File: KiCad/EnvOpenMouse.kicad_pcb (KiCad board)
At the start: 2 copper layers, 28.6 x 94.8 mm, 58 parts, among them J8 TSA343G00-250J2, J9 C145960, Q1 SI2301B, SW1 SW_Push_SPDT, SW2 SW_Push_SPDT, SW3 SW_Push_SPDT, U1 TLV70218DBVR, U2 PMW3360DM-T2QU, U3 SOT-23-5 5.5V 3.3V 500mA, U4 RP2040, Y1 3225_4P

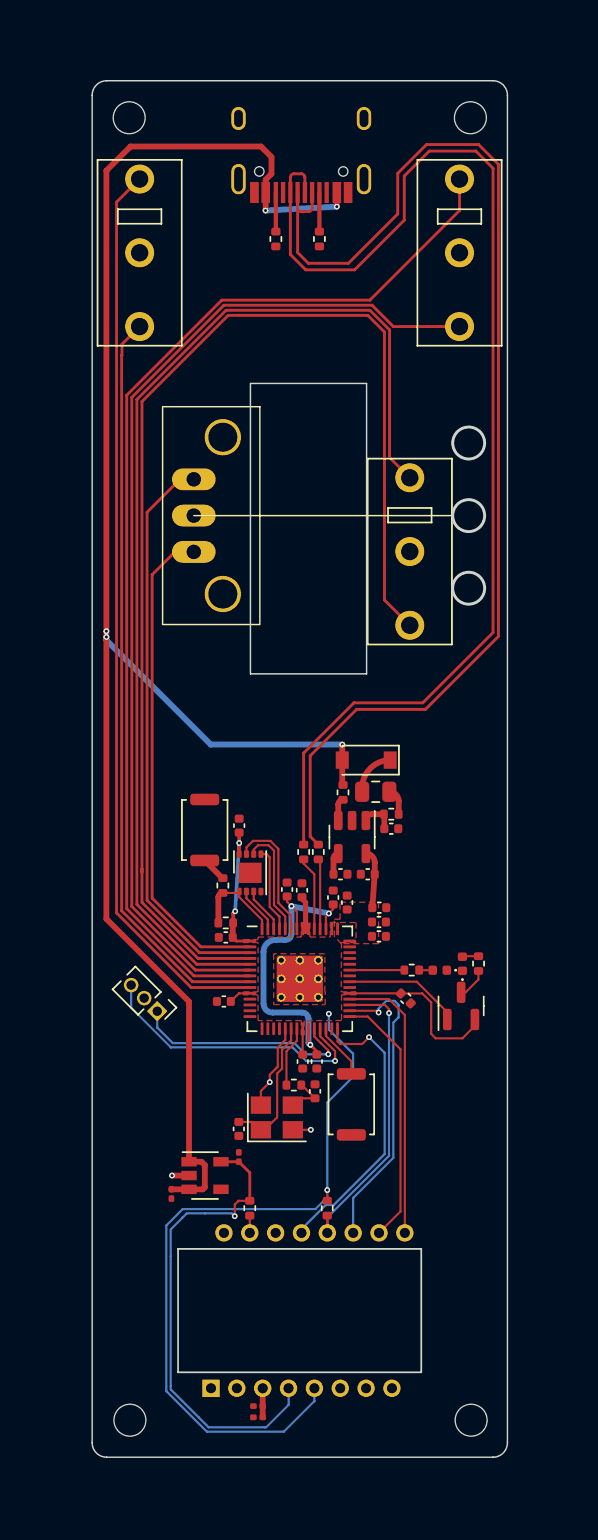
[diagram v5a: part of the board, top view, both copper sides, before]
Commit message: Decided to re-design the whole board again but with a pico so perhaps I can fit a PicoW and maybe make a BLE version
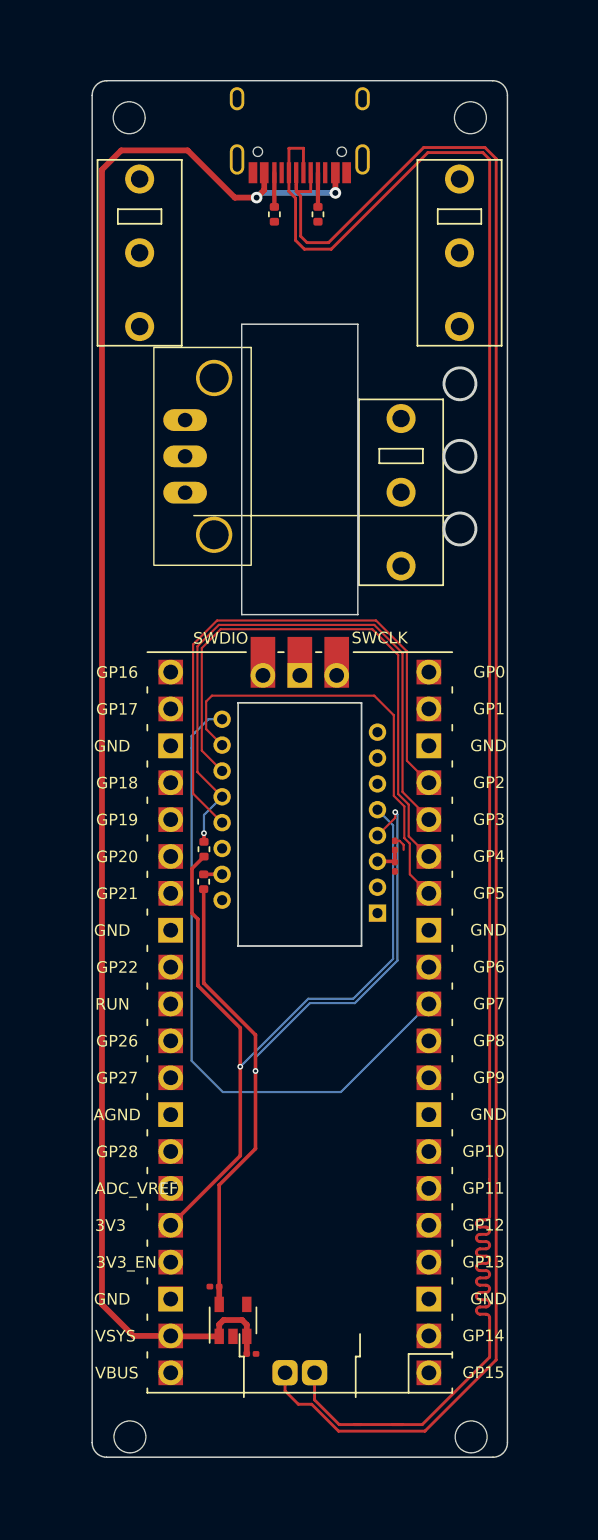
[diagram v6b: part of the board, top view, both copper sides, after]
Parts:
- removed C10, C11, C12, C13, C14, C15, C16, C19, C8, C9: 100nf 0402, Capacitor_SMD:C_0402_1005Metric
- removed C17, C18: 1uf 0402, Capacitor_SMD:C_0402_1005Metric
- removed C20, C5, C6, CBP1: 10uf 0402, Capacitor_SMD:C_0402_1005Metric
- removed C21, C22: 22pf 0402, Capacitor_SMD:C_0402_1005Metric
- removed D1: 1N4002W, Diode_SMD:D_SOD-123
- removed F1: 0805L050WR, Fuse:Fuse_0805_2012Metric
- removed FB1: FerriteBead 0402, Resistor_SMD:R_0402_1005Metric
- removed FLASH1: W25Q16JVUXIQ, Package_SON:SON-8-1EP_3x2mm_P0.5mm_EP1.4x1.6mm
- removed GP23_LED1: GP23 LED_0402, LED_SMD:LED_0402_1005Metric
- removed GPIO24_RESISTOR1, R14, R15: 1K 0402, Resistor_SMD:R_0402_1005Metric
- removed GPIO25_LED1: LED_0402, LED_SMD:LED_0402_1005Metric
- removed GPIO25_RESISTOR1: 470 0402, Resistor_SMD:R_0402_1005Metric
- removed J8, RSW1: TSA343G00-250J2, Button_Switch_SMD:SW_Push_SPST_NO_Alps_SKRK
- removed J9: C145960, Connector_PinHeader_1.27mm:PinHeader_1x03_P1.27mm_Vertical
- removed Q1: SI2301B, Package_TO_SOT_SMD:SOT-23
- removed R11, R12: 27r 0402 resistor, Resistor_SMD:R_0402_1005Metric
- removed R13: 10K 0402, Resistor_SMD:R_0402_1005Metric
- removed R3, R7: 5.1K 0402, Resistor_SMD:R_0402_1005Metric
- removed R8: 100K 0402, Resistor_SMD:R_0402_1005Metric
- removed U3: SOT-23-5 5.5V 3.3V 500mA, Package_TO_SOT_SMD:SOT-23-5
- removed U4: RP2040, RP2040_minimal:RP2040-QFN-56
- removed USB1: TYPE-C-31-M-12, HRO-TYPE-C31-M-12:HRO-TYPE-C-31-M-12
- removed Y1: 3225_4P, Crystal:Crystal_SMD_3225-4Pin_3.2x2.5mm
- added R101: 5.1K 0402, Resistor_SMD:R_0402_1005Metric, F.Cu at (44.5, 29.9)
- added R102: 5.1K 0402, Resistor_SMD:R_0402_1005Metric, F.Cu at (41.5, 29.9)
- added U101: Pico, env:RPi_Pico_SMD_TH_MODIFIED, F.Cu at (43.3, 85.6)
- added USB101: HRO-TYPE-C-31-M-12, Type-C:HRO-TYPE-C-31-M-12, F.Cu at (43.3, 19.4)
- moved C4 40.5 mm to (49.8, 73.4), turned to 90 degrees
- moved C3 38.3 mm to (49.9, 74.9), turned to -90 degrees
- moved U2 32.4 mm to (47.5, 79.6), turned to 180 degrees
- moved R2 26.1 mm to (36.7, 73.7), turned to 90 degrees
- moved R1 22.7 mm to (36.7, 75.9), turned to 90 degrees
- moved C1 12.3 mm to (40.0, 108.4), turned to 180 degrees
- moved U1 10.2 mm to (38.7, 106.1), turned to 90 degrees
- moved C2 9.07 mm to (37.4, 103.8), turned to 0 degrees
- moved SW1 4.12 mm to (50.3, 49.1)
- moved VR1 4.12 mm to (35.4, 46.6)
- moved H3 1.15 mm to (55.1, 114.2)
- moved H4 1.15 mm to (31.6, 114.2)
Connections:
- net MISO/GPIO4 renamed MISO
- U2 pad 10: SCLK/GPIO2 -> SCLK
- U2 pad 11: MOSI/GPIO3 -> MOSI
- U2 pad 13: NCS/GPIO9 -> NCS
- U2 pad 9: MOTION/GPIO1 -> MOTION
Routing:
- net MB-1-A: track 84.3 -> 0.00 mm
- net MB-2-B: track 76.1 -> 0.00 mm
- net MB-1-B: track 75.5 -> 0.00 mm
- net MB-2-A: track 70.8 -> 0.00 mm
- net MB-3-B: track 62.5 -> 0.00 mm
- net USB_D+: track 82.4 -> 137.6 mm
- net MB-3-A: track 51.6 -> 0.00 mm
- net MOTION: track 0.00 -> 44.7 mm
- net USB_D-: track 82.5 -> 125.6 mm
- net ROT-A: track 39.5 -> 0.00 mm
- net NCS: track 0.00 -> 39.1 mm
- net MOSI: track 0.00 -> 38.6 mm
- net ROT-B: track 33.9 -> 0.00 mm
- net SCLK: track 0.00 -> 30.4 mm
- net +3V3: track 82.4 -> 53.4 mm, vias 4 -> 1
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- removed copper zone on F.Cu, net +3V3
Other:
- outline, holes or cut-outs redrawn

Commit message: routed and adjusted various traces and component positions
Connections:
- U101 pad 21: unconnected-(U101-GPIO16-Pad21) -> ROT-B
- U101 pad 22: unconnected-(U101-GPIO17-Pad22) -> ROT-A
- U101 pad 24: unconnected-(U101-GPIO18-Pad24) -> MB-1-A
- U101 pad 25: unconnected-(U101-GPIO19-Pad25) -> MB-1-B
- U101 pad 26: unconnected-(U101-GPIO20-Pad26) -> MB-2-A
- U101 pad 27: unconnected-(U101-GPIO21-Pad27) -> MB-2-B
- U101 pad 29: unconnected-(U101-GPIO22-Pad29) -> MB-3-A
- U101 pad 31: unconnected-(U101-GPIO26_ADC0-Pad31) -> MB-3-B
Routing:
- net MB-2-B: track 0.00 -> 66.0 mm
- net MB-1-A: track 0.00 -> 65.3 mm
- net MB-3-B: track 0.00 -> 62.8 mm
- net MB-2-A: track 0.00 -> 60.0 mm
- net MB-1-B: track 0.00 -> 59.0 mm
- net MB-3-A: track 0.00 -> 47.0 mm
- net ROT-A: track 0.00 -> 22.6 mm
- net ROT-B: track 0.00 -> 13.8 mm
- net MOSI: track 38.6 -> 30.2 mm
- net USB_D+: track 137.6 -> 140.6 mm
- net USB_D-: track 125.6 -> 128.4 mm
- net NCS: track 39.1 -> 38.5 mm
- net MISO: track 42.4 -> 41.9 mm
- net GND: vias 0 -> 2
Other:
- board text added: "Envious.Design"
- board text added: "env"

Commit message: overhauled design and generated gerbers
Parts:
- removed R101, R102: 5.1K 0402, Resistor_SMD:R_0402_1005Metric
- removed U101: Pico, env:RPi_Pico_SMD_TH_MODIFIED
- removed USB101: HRO-TYPE-C-31-M-12, Type-C:HRO-TYPE-C-31-M-12
- added BT1: Li-Po Battery, Connector_JST:JST_PH_B2B-PH-K_1x02_P2.00mm_Vertical, F.Cu at (48.9, 79.3)
- added C10: 100nf 0402, Capacitor_SMD:C_0402_1005Metric, F.Cu at (59.8, 33.5)
- added C11: 100nf 0402, Capacitor_SMD:C_0402_1005Metric, F.Cu at (61.3, 34.9)
- added C12: 100nf 0402, Capacitor_SMD:C_0402_1005Metric, F.Cu at (63.4, 47.7)
- added C13: 100nf 0402, Capacitor_SMD:C_0402_1005Metric, F.Cu at (67.6, 39.0)
- added C14: 100nf 0402, Capacitor_SMD:C_0402_1005Metric, F.Cu at (70.8, 43.7)
- added C15: 100nf 0402, Capacitor_SMD:C_0402_1005Metric, F.Cu at (62.4, 47.7)
- added C16: 100nf 0402, Capacitor_SMD:C_0402_1005Metric, F.Cu at (55.8, 42.9)
- added C17: 100nf 0402, Capacitor_SMD:C_0402_1005Metric, F.Cu at (57.4, 38.8)
- added C18: 100nf 0402, Capacitor_SMD:C_0402_1005Metric, F.Cu at (62.3, 35.0)
- added C19: 100nf 0402, Capacitor_SMD:C_0402_1005Metric, F.Cu at (67.6, 38.0)
- added C20: 1uf 0402, Capacitor_SMD:C_0402_1005Metric, F.Cu at (65.4, 36.8)
- added C21: 1uf 0402, Capacitor_SMD:C_0402_1005Metric, F.Cu at (64.5, 36.8)
- added C22: 22pf 0402, Capacitor_SMD:C_0402_1005Metric, F.Cu at (63.5, 50.8)
- added C23: 22pf 0402, Capacitor_SMD:C_0402_1005Metric, F.Cu at (60.2, 54.1)
- added C5: 10uf 0402 6.3V, Capacitor_SMD:C_0402_1005Metric, F.Cu at (48.4, 27.3)
- added C6: 10uf 0402, Capacitor_SMD:C_0402_1005Metric, F.Cu at (48.3, 22.5)
- added C7: 4.7uf 0402, Capacitor_SMD:C_0402_1005Metric, F.Cu at (50.5, 27.4)
- added C8: 100nf 0402, Capacitor_SMD:C_0402_1005Metric, F.Cu at (69.6, 76.2)
- added C9: 4.7uf 0402, Capacitor_SMD:C_0402_1005Metric, F.Cu at (69.6, 75.1)
- added D1: 1n4002W, Diode_SMD:D_SOD-123, F.Cu at (65.8, 30.4)
- added D2: 0402 led, LED_SMD:LED_0402_1005Metric, F.Cu at (54.0, 30.2)
- added D3: 0402 led, LED_SMD:LED_0402_1005Metric, F.Cu at (55.0, 30.2)
- added FLASH1: W25Q16JVUXIQ, Package_SON:SON-8-1EP_3x2mm_P0.5mm_EP1.4x1.6mm, F.Cu at (57.4, 34.7)
- added J1: Button, Button_Switch_SMD:SW_Push_SPST_NO_Alps_SKRK, F.Cu at (71.8, 23.9)
- added J2: SKRKAEE020, Button_Switch_SMD:SW_Push_SPST_NO_Alps_SKRK, F.Cu at (67.0, 51.2)
- added J3: Conn_01x05, Connector_PinHeader_2.54mm:PinHeader_1x05_P2.54mm_Vertical, F.Cu at (77.6, 65.6)
- added J4: Conn_01x09, Connector_PinHeader_2.54mm:PinHeader_1x09_P2.54mm_Vertical, F.Cu at (77.6, 72.6)
- added J5: Conn_02x02_Top_Bottom, Connector_PinHeader_1.27mm:PinHeader_2x02_P1.27mm_Vertical, F.Cu at (48.4, 129.3)
- added J6: Conn_02x02_Top_Bottom, Connector_PinHeader_1.27mm:PinHeader_2x02_P1.27mm_Vertical, F.Cu at (77.9, 129.3)
- added J7: Conn_02x02_Top_Bottom, Connector_PinHeader_1.27mm:PinHeader_2x02_P1.27mm_Vertical, F.Cu at (48.3, 49.2)
- added J8: Conn_02x02_Top_Bottom, Connector_PinHeader_1.27mm:PinHeader_2x02_P1.27mm_Vertical, F.Cu at (77.9, 49.2)
- added J9: Conn_01x03, Connector_PinHeader_1.27mm:PinHeader_1x03_P1.27mm_Vertical, F.Cu at (63.8, 58.0)
- added R10: 1.18K 0402, Resistor_SMD:R_0402_1005Metric, F.Cu at (56.3, 25.1)
- added R11: 1.13K 0402, Resistor_SMD:R_0402_1005Metric, F.Cu at (51.6, 23.1)
- added R12: 10K 0402, Resistor_SMD:R_0402_1005Metric, F.Cu at (57.3, 32.8)
- added R13: 1K 0402, Resistor_SMD:R_0402_1005Metric, F.Cu at (57.4, 31.7)
- added R14: 27Ohms 0402 Resistor, Capacitor_SMD:C_0402_1005Metric, F.Cu at (62.1, 33.0)
- added R15: 27Ohms 0402 Resistor, Capacitor_SMD:C_0402_1005Metric, F.Cu at (63.4, 32.9)
- added R16: 1K 0402, Resistor_SMD:R_0402_1005Metric, F.Cu at (62.0, 49.6)
- added R3: 10k 0402, Resistor_SMD:R_0402_1005Metric, F.Cu at (48.4, 26.3)
- added R4: 10K 0402, Resistor_SMD:R_0402_1005Metric, F.Cu at (54.9, 71.2)
- added R5: 5.1K, Resistor_SMD:R_0402_1005Metric, F.Cu at (68.4, 24.4)
- added R6: 10K 0402, Resistor_SMD:R_0402_1005Metric, F.Cu at (50.6, 23.1)
- added R7: 1.5K 0402, Resistor_SMD:R_0402_1005Metric, F.Cu at (54.0, 32.1)
- added R8: 5.1K, Resistor_SMD:R_0402_1005Metric, F.Cu at (68.4, 23.4)
- added R9: 1.5K 0402, Resistor_SMD:R_0402_1005Metric, F.Cu at (55.0, 32.1)
- added U3: BQ24074RGT, Package_DFN_QFN:VQFN-16-1EP_3x3mm_P0.5mm_EP1.6x1.6mm, F.Cu at (53.2, 26.6)
- added U4: PMW3360DM-T2QU, local:DIP-16_W10.16mm, F.Cu at (66.8, 80.7)
- added U5: RP2040, RP2040_minimal:RP2040-QFN-56, F.Cu at (62.5, 41.9)
- added Y1: 3225_4P 12MHz, Crystal:Crystal_SMD_3225-4Pin_3.2x2.5mm, F.Cu at (60.8, 51.9)
- added e1: TYPE-C-31-M-12, HRO-TYPE-C31-M-12:HRO-TYPE-C-31-M-12, F.Cu at (62.5, 19.4)
- C1: value 0.1uf 0402 -> 0402 1uF; footprint Capacitor_SMD:C_0201_0603Metric -> Capacitor_SMD:C_0402_1005Metric
- C2: value 1uf 0402 -> 0.1uf 0402; footprint Capacitor_SMD:C_0201_0603Metric -> Capacitor_SMD:C_0402_1005Metric
- C3: value 100nf 0402 -> 1uf 0402; footprint Capacitor_SMD:C_0201_0603Metric -> Capacitor_SMD:C_0402_1005Metric
- C4: value 4.7uf 0402 -> 0402 10uF; footprint Capacitor_SMD:C_0201_0603Metric -> Resistor_SMD:R_0402_1005Metric
- R2: value 10K 0402 -> 4.12K 0402
- U1: value TLV70218DBVR -> TLV75733PDBVR; footprint Package_TO_SOT_SMD:SOT-23-5 -> Package_SON:WSON-6-1EP_2x2mm_P0.65mm_EP1x1.6mm
- U2: value PMW3360DM-T2QU -> TLV70218DBVR; footprint local:DIP-16_W10.16mm -> Package_TO_SOT_SMD:SOT-23-5
- moved SW3 85.8 mm to (73.5, 107.8)
- moved C1 85.7 mm to (54.6, 24.0), turned to 0 degrees
- moved U1 82.4 mm to (48.4, 24.3), turned to -90 degrees
- moved SW1 77.1 mm to (72.0, 123.1)
- moved VR1 77.0 mm to (55.0, 121.1), turned to 90 degrees
- moved H1 76.8 mm to (48.0, 98.3)
- moved C2 76.1 mm to (48.4, 28.4)
- moved H3 75.7 mm to (48.0, 38.8)
- moved SW2 75.2 mm to (51.6, 107.8)
- moved R2 53.0 mm to (52.6, 23.1), turned to -90 degrees
- moved U2 48.5 mm to (47.9, 31.1), turned to -90 degrees
- moved H4 48.0 mm to (76.9, 98.3)
- moved C4 47.7 mm to (56.3, 26.2), turned to 180 degrees
- moved C3 41.2 mm to (48.4, 33.7), turned to 0 degrees
- moved H2 22.0 mm to (77.0, 23.4)
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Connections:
- C1 pad 1: GND -> VSYS
- C1 pad 2: VBUS -> GND
- C2 pad 2: +1V8 -> VDD
- C3 pad 1: Net-(U2-VDDPIX) -> GND
- C3 pad 2: GND -> +1V8
- C4 pad 1: Net-(U2-VDDPIX) -> GND
- C4 pad 2: GND -> VDD
- R1 pad 2: Net-(U2-LED_P) -> Net-(U4-LED_P)
- R2 pad 1: +3V3 -> GND
- R2 pad 2: MISO -> Net-(U3-ITERM)
- U1 pad 1: VBUS -> +3V3
- U1 pad 2: GND -> unconnected-(U1-NC-Pad2)
- U1 pad 3: VBUS -> GND
- U1 pad 4: unconnected-(U1-NC-Pad4) -> Net-(U1-EN)
- U1 pad 5: +1V8 -> unconnected-(U1-NC-Pad5)
- U2 pad 1: unconnected-(U2-NC-Pad1) -> VDD
- U2 pad 2: unconnected-(U2-NC-Pad2) -> GND
- U2 pad 3: Net-(U2-VDDPIX) -> VDD
- U2 pad 4: +1V8 -> unconnected-(U2-NC-Pad4)
- U2 pad 5: +3V3 -> +1V8
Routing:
- net VDD: track 0.00 -> 135.7 mm, vias 0 -> 3
- net USB_D+: track 140.6 -> 9.23 mm
- net +3V3: track 53.4 -> 178.8 mm, vias 1 -> 4
- net USB_D-: track 128.4 -> 8.80 mm
- net VBUS: track 113.1 -> 10.8 mm
- net MB-1-A: track 65.3 -> 5.19 mm
- net VBAT: track 0.00 -> 58.5 mm, vias 0 -> 1
- net BLE_IRQ: track 0.00 -> 49.4 mm, vias 0 -> 2
- net BLE_SCK: track 0.00 -> 49.2 mm
- net BLE_RST: track 0.00 -> 48.3 mm
- net BLE_DFU: track 0.00 -> 48.2 mm, vias 0 -> 2
- net MB-2-A: track 60.0 -> 16.9 mm
- net BLE_CS: track 0.00 -> 42.5 mm
- net BLE_MOSI: track 0.00 -> 40.4 mm
- net +1V8: track 57.0 -> 95.7 mm
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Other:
- board size 28.6 x 94.8 mm -> 34 x 110.1 mm
- board text added: "SWC/GND/SWD"
- board text removed: "Envious.Design"
- board text removed: "env"
